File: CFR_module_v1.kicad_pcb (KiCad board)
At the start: 2 copper layers, 51 parts, among them J1 Conn_01x20, J2 Conn_01x20

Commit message: pcb ok
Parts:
- removed R2, R3: 1k, Resistor_SMD:R_0805_2012Metric_Pad1.20x1.40mm_HandSolder
- C4, C5, C6: footprint Capacitor_THT:CP_Radial_D6.3mm_P2.50mm -> Capacitor_SMD:CP_Elec_6.3x7.7
- D1, D2, D3, D4, D5, D6, F1, F2, F3, R1: moved to B.Cu
- moved R1 106.7 mm to (100.3, 83.4), turned to -90 degrees
- moved IO1 106.6 mm to (126.5, 130.5), turned to 90 degrees
- moved D1 105.2 mm to (131.0, 128.0), turned to -90 degrees
- moved JP7 100.3 mm to (134.0, 124.8), turned to 0 degrees
- moved JP4 97.6 mm to (89.8, 114.4), turned to 180 degrees
- moved JP3 97.0 mm to (85.8, 114.4), turned to 180 degrees
- moved JP6 94.6 mm to (124.8, 110.4), turned to 180 degrees
- moved ALM4 94.3 mm to (136.3, 69.9)
- moved JP2 90.7 mm to (89.4, 94.5), turned to 180 degrees
- moved JP1 89.8 mm to (85.8, 94.4), turned to 180 degrees
- moved JP12 79.1 mm to (129.3, 74.4), turned to 180 degrees
- moved DR2 75.9 mm to (69.5, 102.5)
- moved MOT2 75.9 mm to (66.0, 115.2)
- moved DR1 75.8 mm to (69.5, 80.0)
- moved MOT1 75.8 mm to (66.0, 92.7)
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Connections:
- ALM1 pad 2: GND -> GNDPWR1
- ALM2 pad 2: GND -> GNDPWR2
- ALM3 pad 2: GND -> GNDPWR2
- C1 pad 1: GND -> GNDPWR1
- C2 pad 1: GND -> GNDPWR2
- C3 pad 1: GND -> GNDPWR2
- C4 pad 2: GND -> GNDPWR1
- C5 pad 2: GND -> GNDPWR1
- C6 pad 2: GND -> GNDPWR1
- D1 pad 2: GND -> GNDPWR2
- D2 pad 2: GND -> GNDPWR2
- D3 pad 2: GND -> GNDPWR2
- D4 pad 2: GND -> GNDPWR2
- D5 pad 2: GND -> GNDPWR2
- DR1 pad 10: +3V3_Pico -> GND
- DR1 pad 7: GND -> GNDPWR1
- DR2 pad 10: +3V3_Pico -> GND
- DR2 pad 11: GND -> +3V3_Pico
- DR2 pad 7: GND -> GNDPWR1
- DR3 pad 15: GP21 -> GP19
- DR3 pad 16: GP22 -> GP18
- DR3 pad 7: GND -> GNDPWR1
- DR3 pad 9: GP18 -> GP22
- IO1 pad 1: GND -> GNDPWR2
- IO2 pad 1: GND -> GNDPWR2
- IO3 pad 1: GND -> GNDPWR2
- IO4 pad 1: GND -> GNDPWR2
- IO5 pad 1: GND -> GNDPWR2
- JP2 pad 3: GP4 -> unconnected-(JP2-B-Pad3)
- JP4 pad 3: GP4 -> unconnected-(JP4-B-Pad3)
- JP5 pad 1: GP19 -> GP21
- JP6 pad 3: GP4 -> unconnected-(JP6-B-Pad3)
- R1 pad 1: GP5 -> GP4
- R1 pad 2: GP4 -> GP5
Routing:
- net +BATT: track 0.00 -> 177.8 mm, vias 0 -> 1
- net GNDPWR1: track 0.00 -> 170.8 mm, vias 0 -> 1
- net +3V3_Pico: track 0.00 -> 168.5 mm
- net GND: track 0.00 -> 154.8 mm, vias 0 -> 1
- net GNDPWR2: track 0.00 -> 132.5 mm, vias 0 -> 1
- net GP5: track 0.00 -> 100.2 mm
- net +V2: track 0.00 -> 78.6 mm
- net GP2: track 0.00 -> 69.3 mm, vias 0 -> 1
- net +V1: track 0.00 -> 65.7 mm
- net GP3: track 0.00 -> 65.2 mm
- net GP17: track 0.00 -> 31.8 mm
- net GP16: track 0.00 -> 31.5 mm
- net GP27_A1: track 0.00 -> 29.4 mm
- net GP28_A2: track 0.00 -> 29.0 mm
- net +9V: track 0.00 -> 28.3 mm, vias 0 -> 1
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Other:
- board outline added: 88 x 73 mm

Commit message: fini avant modifs
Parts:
- added BAU1: Conn_01x02, Connector_PinHeader_2.54mm:PinHeader_1x02_P2.54mm_Vertical, F.Cu at (85.5, 72.3)
- added D10: D_Schottky, Diode_SMD:D_SOD-123, B.Cu at (103.5, 96.0)
- added D11: D_Schottky, Diode_SMD:D_SOD-123, B.Cu at (97.0, 122.0)
- added D12: D_Schottky, Diode_SMD:D_SOD-123, B.Cu at (124.9, 98.0)
- added D7: D_Schottky, Diode_SMD:D_SOD-123, B.Cu at (107.5, 94.5)
- added D8: D_Schottky, Diode_SMD:D_SOD-123, B.Cu at (107.5, 97.5)
- added D9: D_Schottky, Diode_SMD:D_SOD-123, B.Cu at (124.9, 95.6)
- added G***: LOGO, Visuels_custom:logo_PCB, F.Cu at (78.2, 72.5)
- added H1: MountingHole, MountingHole:MountingHole_3.2mm_M3, F.Cu at (70.5, 70.5)
- added H2: MountingHole, MountingHole:MountingHole_3.2mm_M3, F.Cu at (144.0, 70.5)
- added H3: MountingHole, MountingHole:MountingHole_3.2mm_M3, F.Cu at (70.5, 134.0)
- added H4: MountingHole, MountingHole:MountingHole_3.2mm_M3, F.Cu at (144.0, 134.0)
- added Q1: NPN, Package_TO_SOT_SMD:SOT-23, B.Cu at (108.0, 85.5)
- added R2: 1k, Resistor_SMD:R_0805_2012Metric_Pad1.20x1.40mm_HandSolder, B.Cu at (102.5, 77.5)
- added R3: 10k, Resistor_SMD:R_0805_2012Metric_Pad1.20x1.40mm_HandSolder, B.Cu at (110.0, 80.0)
- added R4: 1k, Resistor_SMD:R_0805_2012Metric_Pad1.20x1.40mm_HandSolder, B.Cu at (101.5, 102.0)
- added R5: 1k, Resistor_SMD:R_0805_2012Metric_Pad1.20x1.40mm_HandSolder, B.Cu at (93.5, 120.5)
- added R6: 1k, Resistor_SMD:R_0805_2012Metric_Pad1.20x1.40mm_HandSolder, B.Cu at (114.0, 96.5)
- PiPico0: renamed from Pico0; footprint Module:RaspberryPi_Pico_Common_Unspecified -> Module:RaspberryPi_Pico_Common_SMD
- moved JP5 10.1 mm to (125.0, 101.0), turned to 0 degrees
- moved JP2 7.97 mm to (89.5, 86.5)
- moved JP3 5.88 mm to (89.5, 119.0)
- moved JP4 5.40 mm to (89.5, 109.0)
- moved IO2 4.72 mm to (140.0, 128.0)
- moved JP1 4.24 mm to (89.5, 96.5)
- moved F1 4.21 mm to (82.5, 131.5)
- moved C5 3.80 mm to (79.5, 116.0)
- moved C4 3.73 mm to (79.5, 94.5)
- moved DR2 3.67 mm to (73.0, 101.5)
- moved MOT2 3.66 mm to (69.5, 114.2)
- moved MOT3 3.66 mm to (145.0, 104.8)
- moved D2 3.62 mm to (137.2, 126.5)
- moved D1 3.55 mm to (127.8, 126.5)
- moved DR1 3.53 mm to (73.0, 80.0)
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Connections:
- C1 pad 1: GNDPWR1 -> +BATT
- C1 pad 2: +BATT -> GNDPWR1
- C2 pad 1: GNDPWR2 -> +9V
- C2 pad 2: +9V -> GNDPWR2
- C3 pad 1: GNDPWR2 -> +5V
- C3 pad 2: +5V -> GNDPWR2
- DR1 pad 9: GP10 -> M1_EN
- DR2 pad 9: GP15 -> M2_EN
- DR3 pad 9: GP22 -> M3_EN
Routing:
- net M2_EN: track 0.00 -> 42.9 mm
- net Net-(D7-A): track 0.00 -> 33.2 mm
- net GND: track 154.8 -> 184.4 mm, vias 1 -> 0
- net M1_EN: track 0.00 -> 23.1 mm, vias 0 -> 1
- net Net-(BAU1-Pin_2): track 0.00 -> 22.3 mm
- net GP5: track 100.2 -> 81.0 mm, vias 0 -> 1
- net +V2: track 78.6 -> 65.8 mm
- net GNDPWR1: track 170.8 -> 159.4 mm, vias 1 -> 2
- net +BATT: track 177.8 -> 167.3 mm
- net Net-(D12-A): track 0.00 -> 10.4 mm
- net Net-(Q1-B): track 0.00 -> 9.82 mm
- net GP15: track 17.3 -> 7.67 mm
- net GP21: track 17.6 -> 9.43 mm
- net GP10: track 18.8 -> 11.5 mm
- net GP22: track 17.6 -> 11.6 mm
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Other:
- board size 88 x 73 mm -> 80.9 x 70.9 mm
- board text added: "(I2C0, UART0)"
- board text added: "(I2C1)"
- board text added: "100uF"
- board text added: "10k"
- board text added: "1k"
- board text added: "330-1000uF"
- board text added: "5V"
- board text added: "5V_pwr"
- board text added: "="
- board text added: "DC"
- board text added: "EN: GP10 IB1: GP8 IB2: GP9 IA1-DIR: GP6 IA2-STEP: GP7 UART: GP5"
- board text added: "EN: GP15 IB1: GP13 IB2: GP14 IA1-DIR: GP11 IA2-STEP: GP12 UART: GP5"
- board text added: "EN: GP22 IB1: GP20 IB2: GP21 IA1-DIR: GP18 IA2-STEP: GP19 UART: GP5"
- board text added: "GND"
- board text added: "GP16"
- board text added: "GP17"
- board text added: "GP2"
- board text added: "GP26"
- board text added: "GP27"
- board text added: "GP28"
- board text added: "GP3"
- board text added: "Raspberry Pi Pico"
- board text added: "SM"
- board text added: "V0"
- board text added: "V1"
- board text added: "V2"
- board text added: "VCC"
- board text added: "VI"
- board text added: "Vbatt"
- board text added: "~100uF"
- board text added: "~220uF"

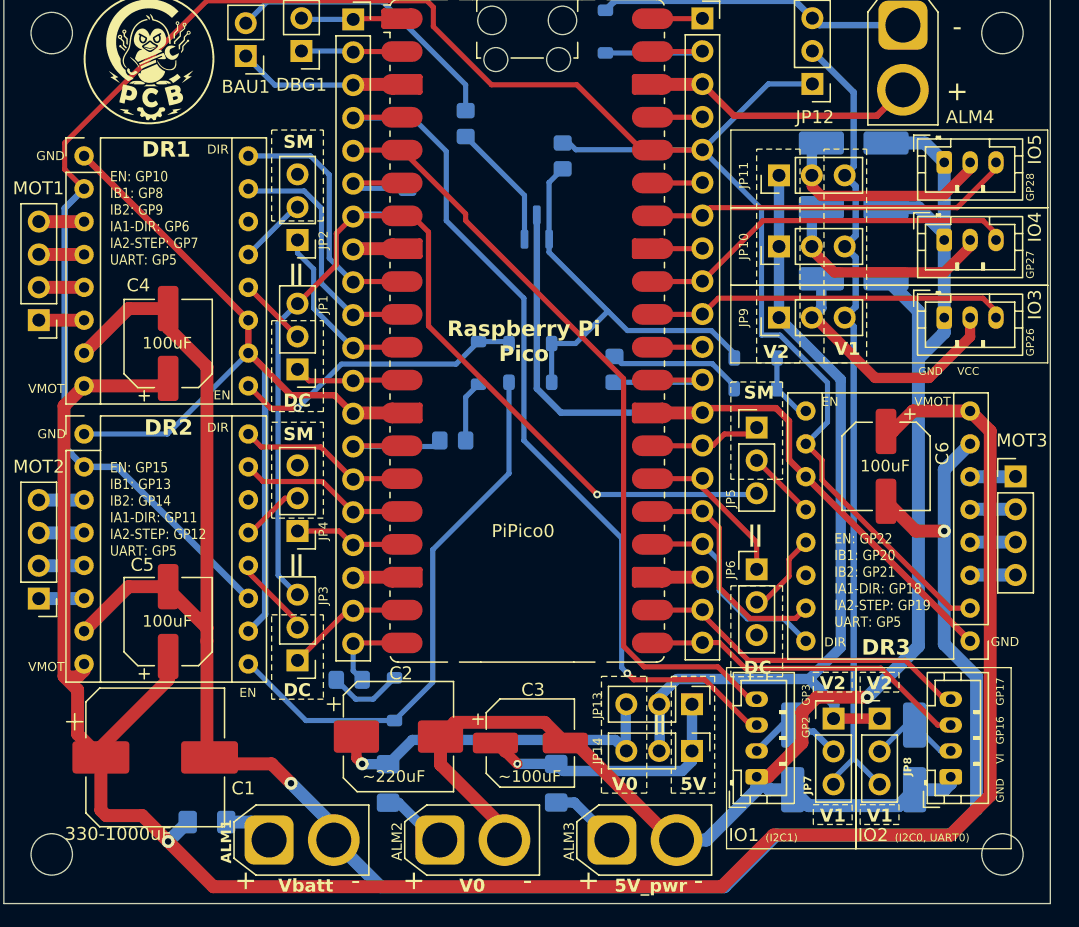
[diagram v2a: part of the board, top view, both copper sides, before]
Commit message: GND commun et ajout de branchements batterie
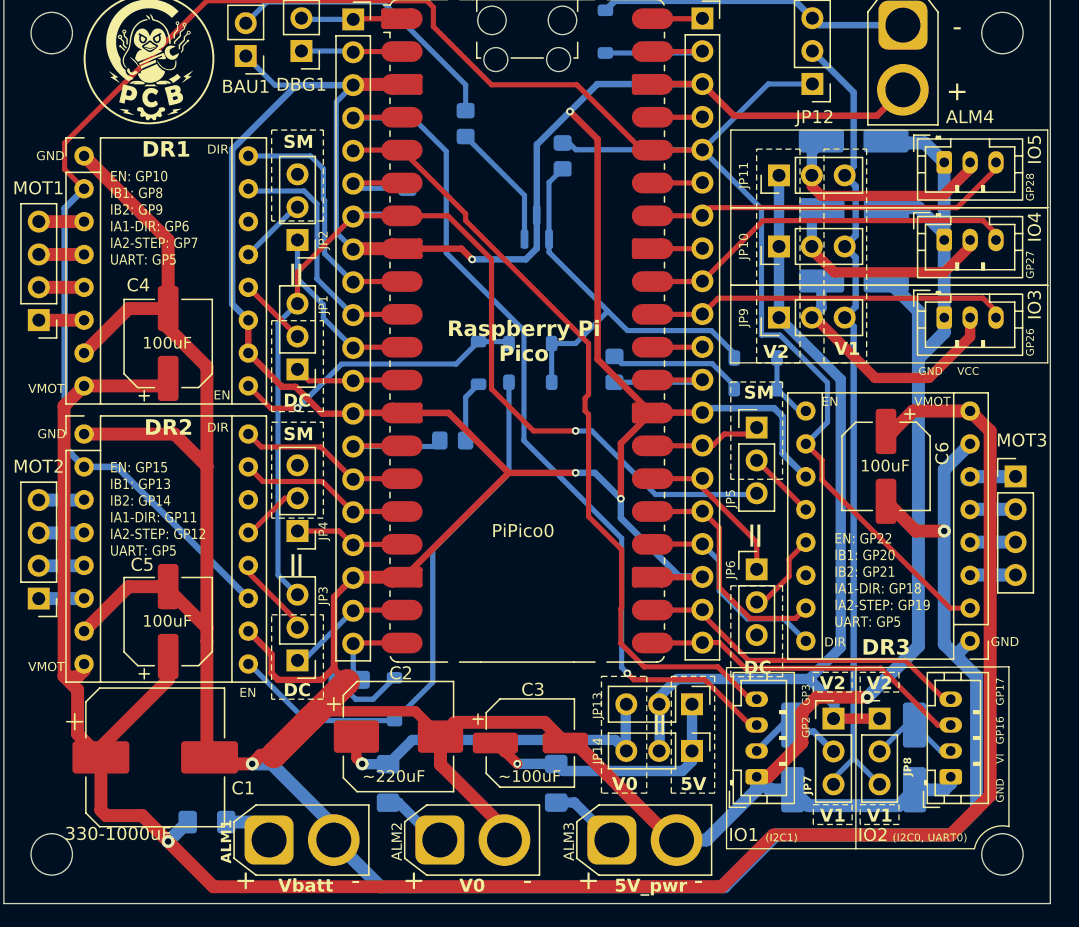
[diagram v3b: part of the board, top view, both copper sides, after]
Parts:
- added NT3: NetTie_3_Tee, NetTie:NetTie-3_SMD_Pad2.0mm, F.Cu at (90.5, 123.5)
- moved D4 0.18 mm to (132.5, 84.2)
- moved D3 0.17 mm to (132.5, 89.7)
- moved D5 0.16 mm to (132.5, 78.8)
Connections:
- DR1 pad 1: GND -> GNDPWR1
- DR2 pad 1: GND -> GNDPWR1
- DR3 pad 1: GND -> GNDPWR1
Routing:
- net GND: track 184.4 -> 246.8 mm, vias 0 -> 4
- net GNDPWR1: track 159.4 -> 188.0 mm
- net GNDPWR2: track 132.8 -> 143.9 mm
- net GP5: track 81.0 -> 82.6 mm

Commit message: liste des composants
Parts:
- added J3: Conn_01x02, Connector_PinHeader_2.54mm:PinHeader_1x02_P2.54mm_Vertical, F.Cu at (70.0, 123.5)
- added J4: Conn_01x02, Connector_PinHeader_2.54mm:PinHeader_1x02_P2.54mm_Vertical, F.Cu at (135.0, 135.1)
- added J5: Conn_01x02, Connector_PinHeader_2.54mm:PinHeader_1x02_P2.54mm_Vertical, F.Cu at (126.8, 135.1)
- moved ALM1 5.21 mm to (92.5, 132.5), turned to 180 degrees
- moved ALM4 5.16 mm to (137.0, 75.0), turned to 90 degrees
- moved ALM2 5.02 mm to (105.5, 132.5), turned to 180 degrees
- moved ALM3 4.71 mm to (118.5, 132.5), turned to 180 degrees
- moved C3 0.89 mm to (107.5, 124.5)
- moved DBG1 0.61 mm to (89.8, 72.5)
- moved BAU1 0.22 mm to (85.5, 72.5)
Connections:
- net +9V renamed +V0
- ALM1 pad 1: Net-(ALM1-Pin_1) -> GNDPWR1
- ALM1 pad 2: GNDPWR1 -> Net-(ALM1-Pin_2)
- ALM2 pad 1: Net-(ALM2-Pin_1) -> GNDPWR2
- ALM2 pad 2: GNDPWR2 -> Net-(ALM2-Pin_2)
- ALM3 pad 1: Net-(ALM3-Pin_1) -> GNDPWR2
- ALM3 pad 2: GNDPWR2 -> Net-(ALM3-Pin_2)
- ALM4 pad 1: +5V_Pico -> GND
- ALM4 pad 2: GND -> +5V_Pico
- F1 pad 2: Net-(ALM1-Pin_1) -> Net-(ALM1-Pin_2)
- F2 pad 2: Net-(ALM2-Pin_1) -> Net-(ALM2-Pin_2)
- F3 pad 2: Net-(ALM3-Pin_1) -> Net-(ALM3-Pin_2)
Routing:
- net +5V: track 20.8 -> 37.9 mm
- net +V0: track 27.5 -> 41.3 mm
- net GNDPWR1: track 188.0 -> 201.7 mm, vias 2 -> 3
- net GNDPWR2: track 143.9 -> 155.8 mm
- net Net-(ALM3-Pin_2): track 0.00 -> 5.51 mm
- net Net-(ALM3-Pin_1): track 5.51 -> 0.00 mm
- net +BATT: track 167.3 -> 172.6 mm
- net Net-(ALM2-Pin_2): track 0.00 -> 4.91 mm
- net Net-(ALM2-Pin_1): track 4.91 -> 0.00 mm
- net Net-(ALM1-Pin_2): track 0.00 -> 3.89 mm
- net Net-(ALM1-Pin_1): track 3.89 -> 0.00 mm
- net +5V_Pico: track 24.1 -> 24.8 mm
- net GND: track 246.8 -> 247.3 mm
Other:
- board text added: "(Pico)"
- board text added: "+5V"
- board text added: "+V0"
- board text added: "+Vbatt"
- board text added: "3V3"
- board text added: "5V_pico"
- board text added: "RX/GP1"
- board text added: "Selct. bus V1"
- board text added: "Selct. bus V2"
- board text added: "TX/GP0"
